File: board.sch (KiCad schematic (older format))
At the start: 1 part

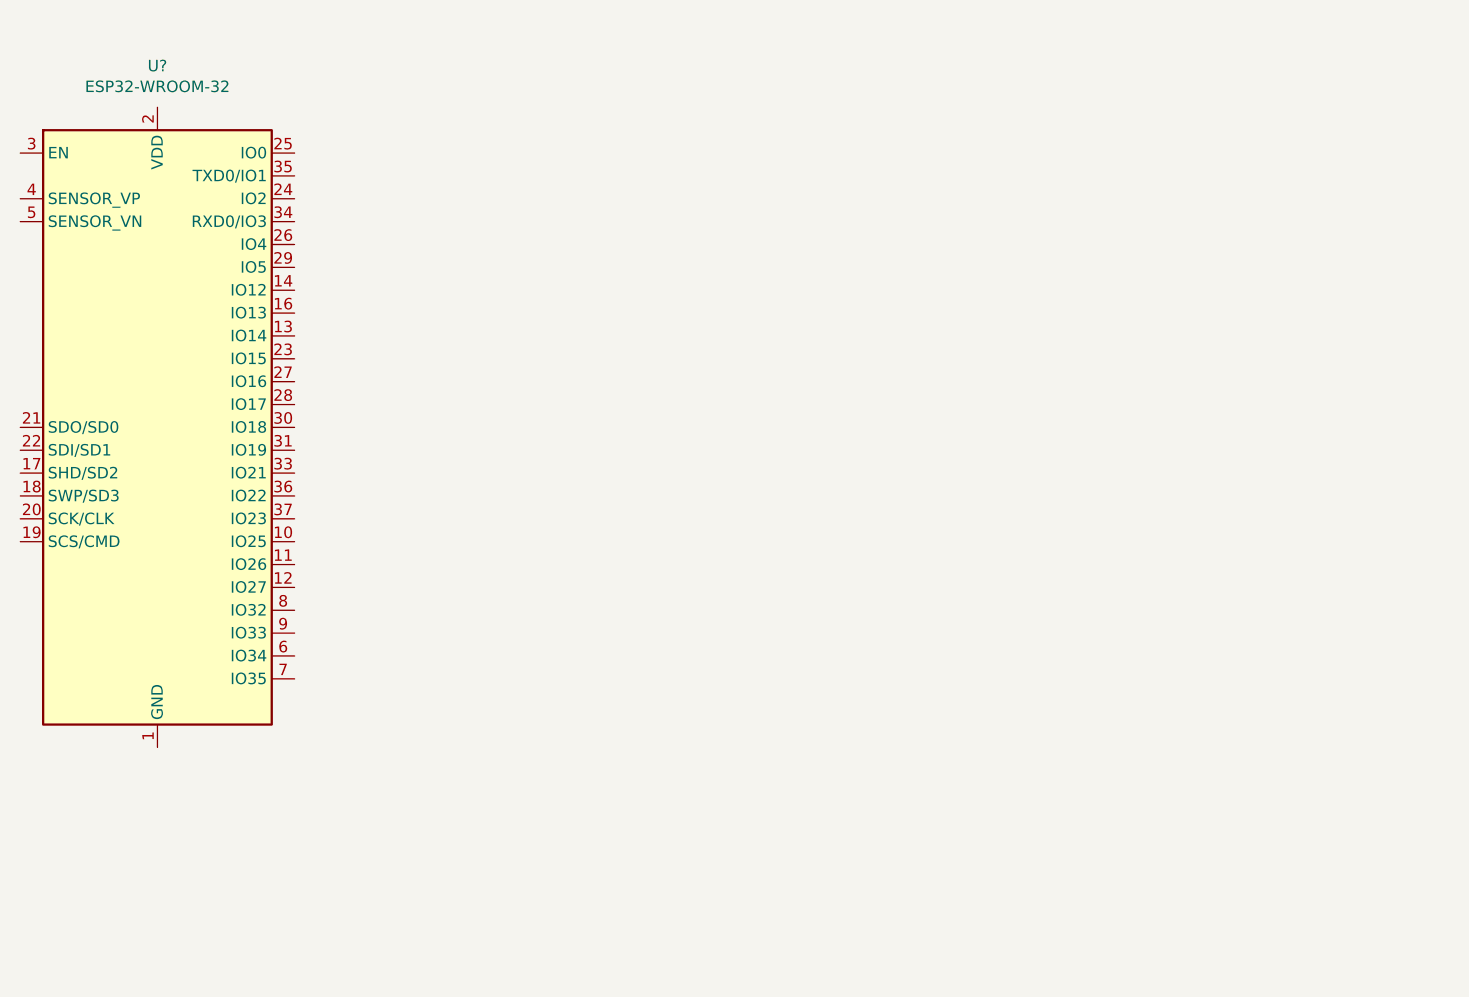
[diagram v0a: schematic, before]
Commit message: added labels
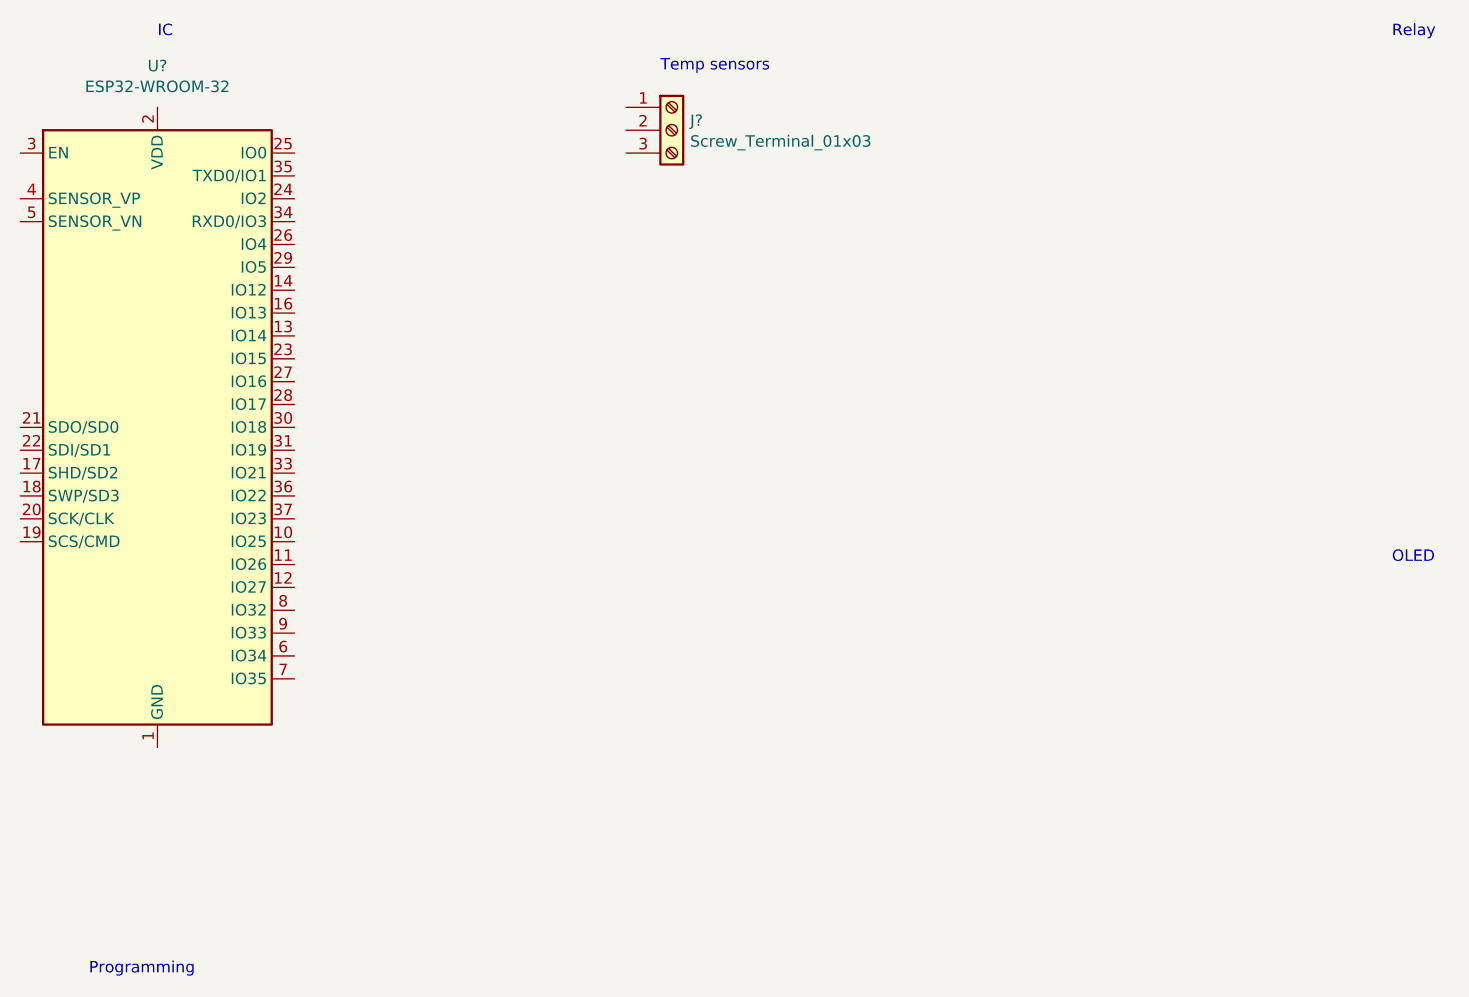
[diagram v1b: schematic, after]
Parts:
- added J?: Screw_Terminal_01x03, symbol Connector:Screw_Terminal_01x03
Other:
- note added: "IC"
- note added: "OLED"
- note added: "Programming"
- note added: "Relay"
- note added: "Temp sensors"
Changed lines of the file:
@@
 	1    0    0    -1
 $EndComp
+$Comp
+L Connector:Screw_Terminal_01x03 J?
+U 1 1 60CDEB35
+P 5950 1750
+F 0 "J?" H 6030 1792 50  0000 L CNN
+F 1 "Screw_Terminal_01x03" H 6030 1701 50  0000 L CNN
+F 2 "" H 5950 1750 50  0001 C CNN
+F 3 "~" H 5950 1750 50  0001 C CNN
+	1    5950 1750
+	1    0    0    -1
+$EndComp
+Text Notes 5900 1500 0    50   ~ 0
+Temp sensors
+Text Notes 3700 1350 0    50   ~ 0
+IC
+Text Notes 9100 1350 0    50   ~ 0
+Relay
+Text Notes 9100 3650 0    50   ~ 0
+OLED
+Text Notes 3400 5450 0    50   ~ 0
+Programming
 $EndSCHEMATC

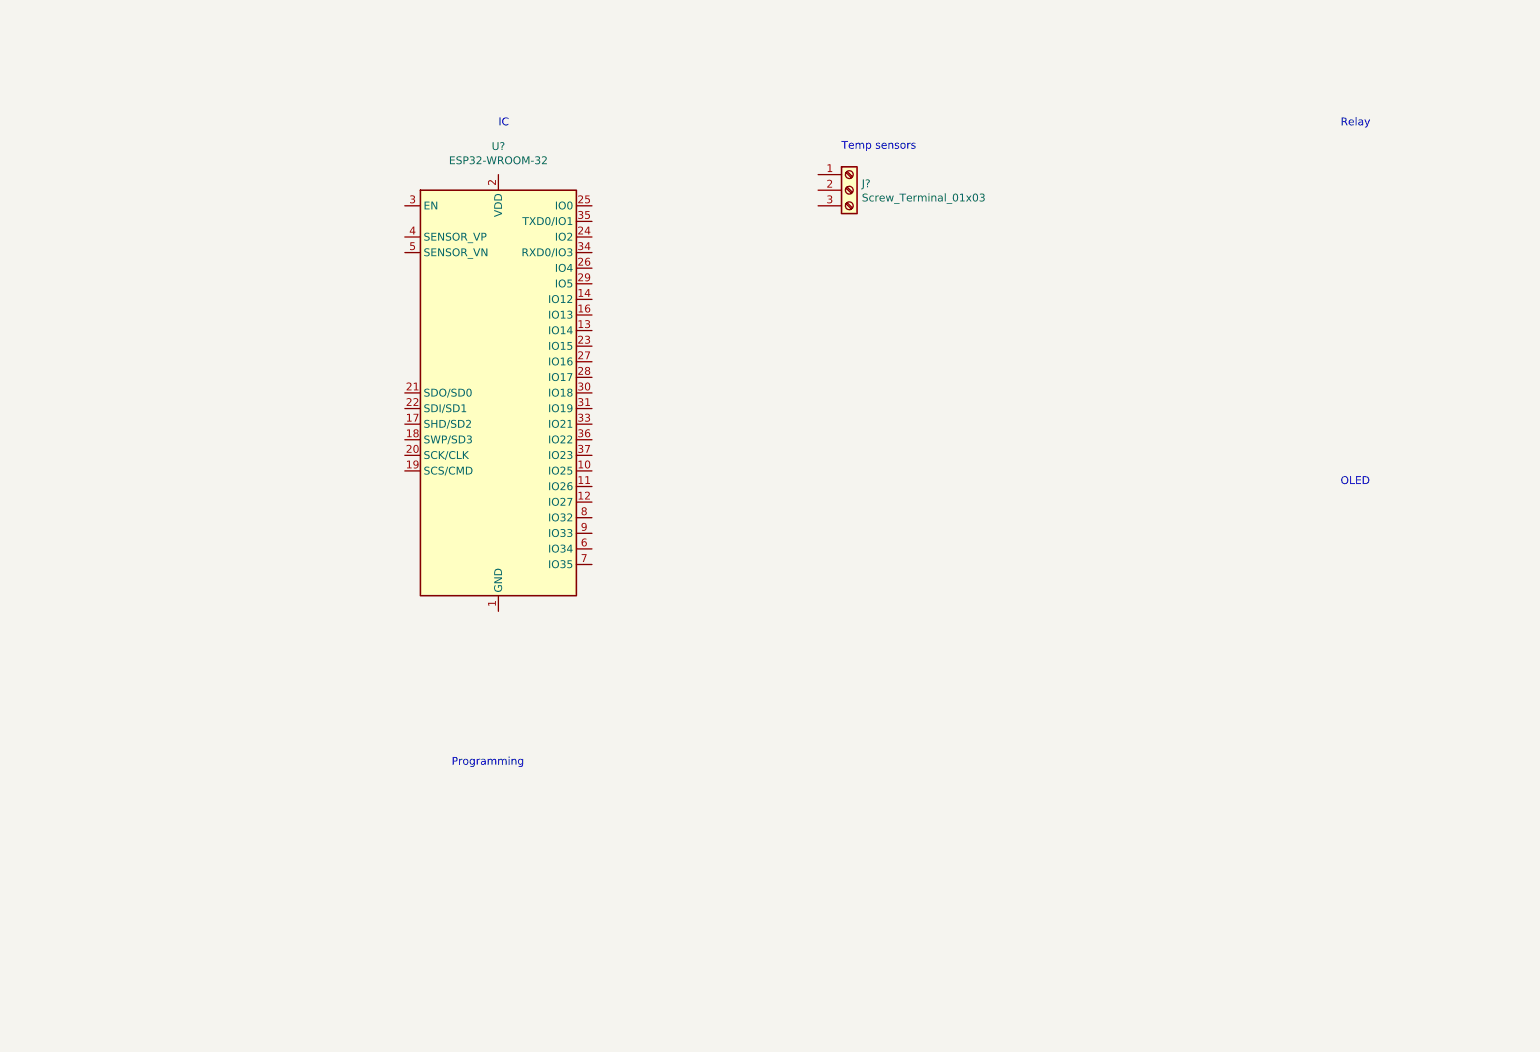
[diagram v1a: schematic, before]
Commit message: initial fiddling with 3d board view
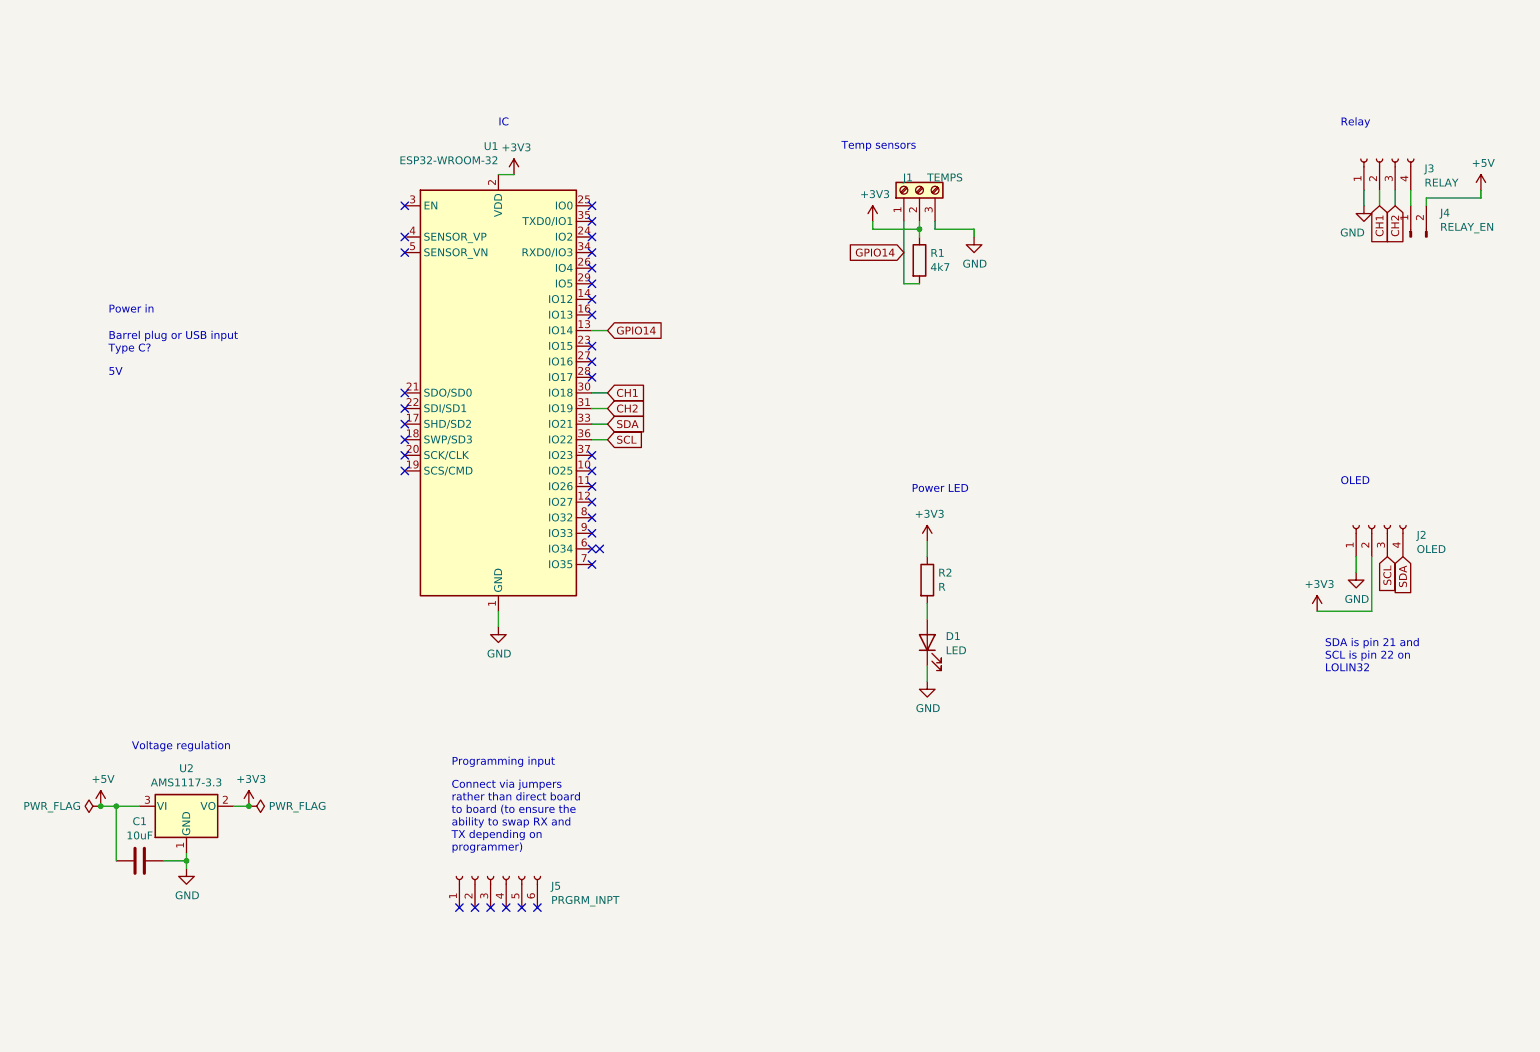
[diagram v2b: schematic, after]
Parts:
- added C1: 10uF, Capacitor_SMD:CP_Elec_3x5.3, symbol Device:C
- added D1: LED, LED_SMD:LED_0201_0603Metric, symbol Device:LED
- added J2: OLED, Connector_JST:JST_EH_B4B-EH-A_1x04_P2.50mm_Vertical, symbol Connector:Conn_01x04_Female
- added J3: RELAY, Connector_JST:JST_EH_B4B-EH-A_1x04_P2.50mm_Vertical, symbol Connector:Conn_01x04_Female
- added J4: RELAY_EN, Connector_PinHeader_2.54mm:PinHeader_1x02_P2.54mm_Vertical, symbol Connector:Conn_01x02_Male
- added J5: PRGRM_INPT, Connector_PinHeader_2.54mm:PinHeader_1x06_P2.54mm_Vertical, symbol Connector:Conn_01x06_Female
- added R1: 4k7, Resistor_SMD:R_0201_0603Metric, symbol Device:R
- added R2: R, Resistor_SMD:R_0201_0603Metric, symbol Device:R
- added U2: AMS1117-3.3, Package_TO_SOT_SMD:SOT-223-3_TabPin2, symbol Regulator_Linear:AMS1117-3.3
- J1: renamed from J?; value Screw_Terminal_01x03 -> TEMPS; footprint (none) -> Connector_JST:JST_EH_S3B-EH_1x03_P2.50mm_Horizontal
- gave numbers to parts that had none: 1
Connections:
- net GND: now reaches U1.1 (GND), U1.15 (GND), U1.38 (GND), U1.39 (GND)
- net GND: now also J1.3 (Pin_3), C1.1, D1.1 (K), J2.1 (Pin_1), J3.1 (Pin_1), U2.1 (GND)
- net GPIO14: now reaches U1.13 (IO14)
- net GPIO14: now also J1.1 (Pin_1), R1.2
- net +3V3: now reaches U1.2 (VDD)
- net +3V3: now also J1.2 (Pin_2), J2.2 (Pin_2), R1.1, R2.1, U2.2 (VO)
- net CH1: now reaches U1.30 (IO18)
- net CH1: now also J3.2 (Pin_2)
- net CH2: now reaches U1.31 (IO19)
- net CH2: now also J3.3 (Pin_3)
- net SDA: now reaches U1.33 (IO21)
- net SDA: now also J2.4 (Pin_4)
- net SCL: now reaches U1.36 (IO22)
- net SCL: now also J2.3 (Pin_3)
- new net: J3.4 (Pin_4), J4.1 (Pin_1)
- new net: D1.2 (A), R2.2
- new net +5V: C1.2, J4.2 (Pin_2), U2.3 (VI)
- no-connect marks 0 -> 35
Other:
- note added: "5V"
- note added: "Barrel plug or USB input\nType C?"
- note added: "Connect via jumpers \nrather than direct board \nto board (to ensure the \nability to swap RX and \nTX depending on \nprogrammer)"
- note added: "Power LED"
- note added: "Power in"
- note added: "Programming input"
- note added: "SDA is pin 21 and \nSCL is pin 22 on \nLOLIN32\n"
- note added: "Voltage regulation"
- note removed: "Programming"
- moved on the sheet: J1

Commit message: added programmer, usb and general design improvements to schematic and did some measuring for final board
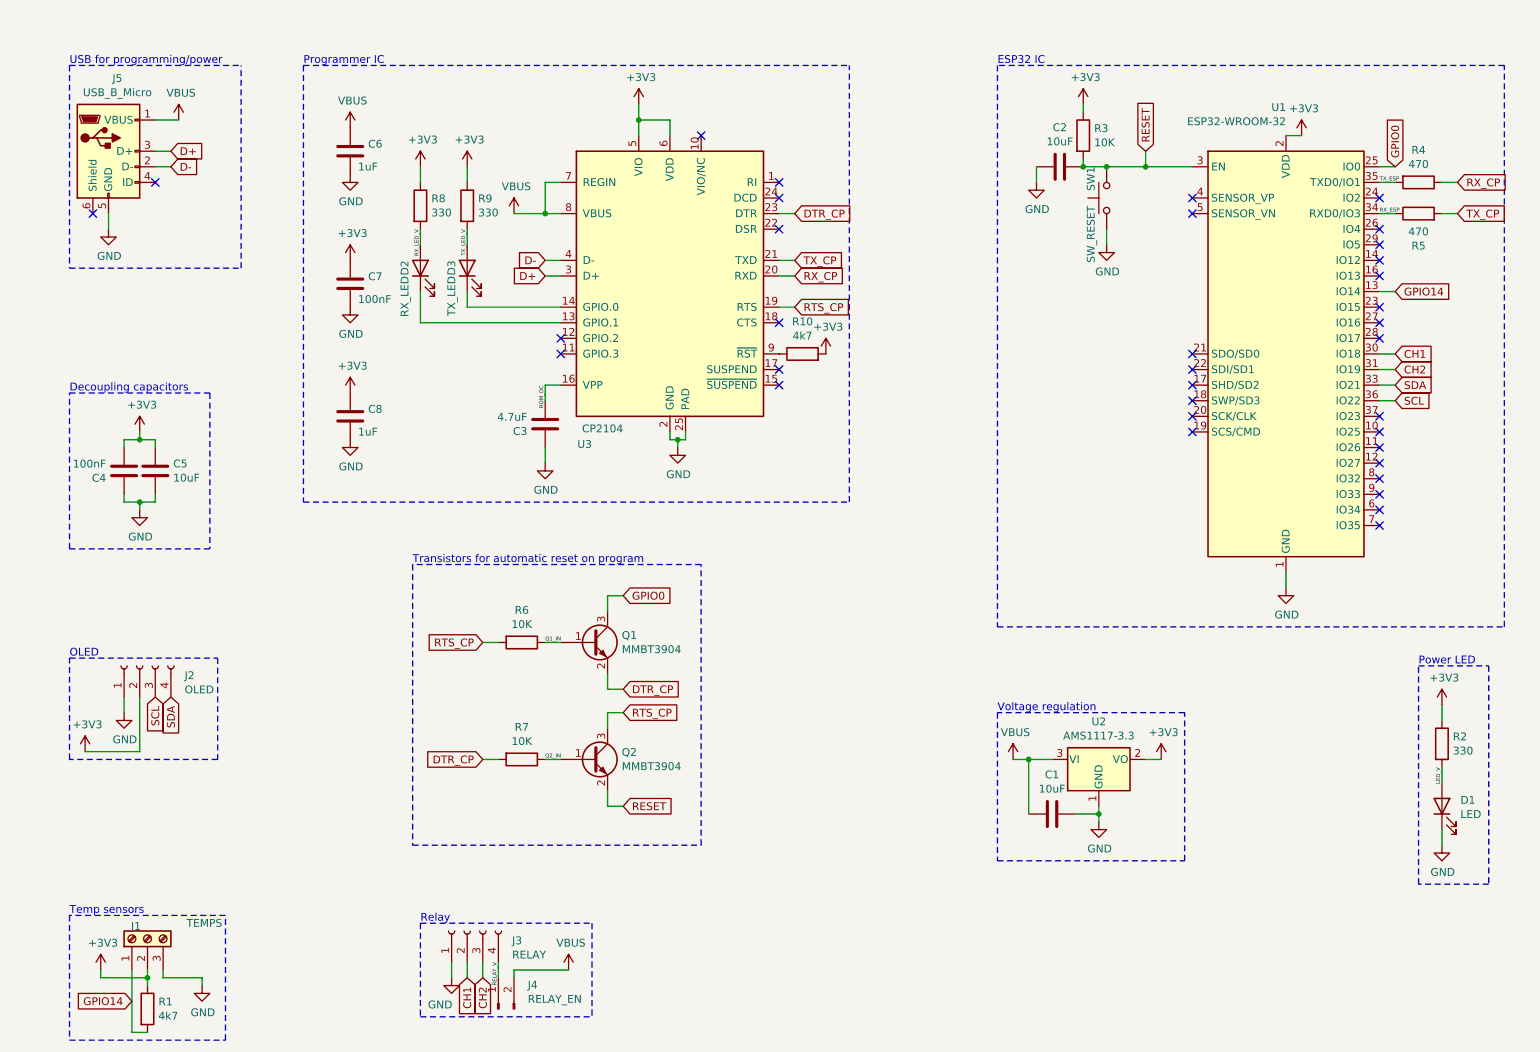
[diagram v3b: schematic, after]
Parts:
- removed J5: PRGRM_INPT, Connector_PinHeader_2.54mm:PinHeader_1x06_P2.54mm_Vertical, symbol Connector:Conn_01x06_Female
- added C2, C5: 10uF, Capacitor_SMD:C_0805_2012Metric, symbol Device:C
- added C3: 4.7uF, Capacitor_SMD:C_0805_2012Metric, symbol Device:C
- added C4, C7: 100nF, Capacitor_SMD:C_0805_2012Metric, symbol Device:C
- added C6, C8: 1uF, Capacitor_SMD:C_0805_2012Metric, symbol Device:C
- added D2: RX_LED, LED_SMD:LED_0805_2012Metric, symbol Device:LED
- added D3: TX_LED, LED_SMD:LED_0805_2012Metric, symbol Device:LED
- added J5: USB_B_Micro, Connector_USB:USB_Micro-B_Molex_47346-0001, symbol Connector:USB_B_Micro
- added Q1, Q2: MMBT3904, Package_TO_SOT_SMD:SOT-23, symbol Transistor_BJT:MMBT3904
- added R10: 4k7, Resistor_SMD:R_0805_2012Metric, symbol Device:R
- added R3, R6, R7: 10K, Resistor_SMD:R_0805_2012Metric, symbol Device:R
- added R4, R5: 470, Resistor_SMD:R_0805_2012Metric, symbol Device:R
- added R8, R9: 330, Resistor_SMD:R_0805_2012Metric, symbol Device:R
- added SW1: SW_RESET, Button_Switch_SMD:SW_SPST_B3U-1000P-B, symbol Switch:SW_Push
- added U3: CP2104, Package_DFN_QFN:QFN-24-1EP_4x4mm_P0.5mm_EP2.6x2.6mm, symbol Interface_USB:CP2104
- C1: footprint Capacitor_SMD:CP_Elec_3x5.3 -> Capacitor_SMD:C_0805_2012Metric
- D1: footprint LED_SMD:LED_0201_0603Metric -> LED_SMD:LED_0805_2012Metric
- J1: footprint Connector_JST:JST_EH_S3B-EH_1x03_P2.50mm_Horizontal -> Connector_JST:JST_XH_B3B-XH-A_1x03_P2.50mm_Vertical
- J2, J3: footprint Connector_JST:JST_EH_B4B-EH-A_1x04_P2.50mm_Vertical -> Connector_JST:JST_XH_B4B-XH-A_1x04_P2.50mm_Vertical
- R1: footprint Resistor_SMD:R_0201_0603Metric -> Resistor_SMD:R_0805_2012Metric
- R2: value R -> 330; footprint Resistor_SMD:R_0201_0603Metric -> Resistor_SMD:R_0805_2012Metric
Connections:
- net +3V3: now also C4.2, C5.1, C7.1, C8.1, R10.2, R3.1, R8.1, R9.1, U3.5 (VIO), U3.6 (VDD)
- net GND: now also C2.1, C3.2, C4.1, C5.2, C6.2, C7.2, C8.2, J5.5 (GND), SW1.1, U3.2 (GND), U3.25 (PAD)
- net GPIO0: now reaches U1.25 (IO0)
- net GPIO0: now also Q1.3 (C)
- net RESET: now reaches U1.3 (EN)
- net RESET: now also C2.2, Q2.2 (E), R3.2, SW1.2
- net RX_ESP: now reaches U1.34 (RXD0/IO3)
- net RX_ESP: now also R5.1
- net TX_ESP: now reaches U1.35 (TXD0/IO1)
- net TX_ESP: now also R4.2
- net RELAY_V: now reaches J3.4 (Pin_4), J4.1 (Pin_1)
- net LED_V: now reaches D1.2 (A), R2.2
- net +5V renamed VBUS
- net VBUS: now also C6.1, J5.1 (VBUS), U3.7 (REGIN), U3.8 (VBUS)
- new net: D2.1 (K), U3.13 (GPIO.1)
- new net: D3.1 (K), U3.14 (GPIO.0)
- new net: R10.1, U3.9 (~RST)
- new net D+: J5.3 (D+), U3.3 (D+)
- new net D-: J5.2 (D-), U3.4 (D-)
- new net DTR_CP: Q1.2 (E), R7.2, U3.23 (DTR)
- new net Q1_IN: Q1.1 (B), R6.1
- new net Q2_IN: Q2.1 (B), R7.1
- new net ROM_DC: C3.1, U3.16 (VPP)
- new net RTS_CP: Q2.3 (C), R6.2, U3.19 (RTS)
- new net RX_CP: R4.1, U3.20 (RXD)
- new net RX_LED_V: D2.2 (A), R8.2
- new net TX_CP: R5.2, U3.21 (TXD)
- new net TX_LED_V: D3.2 (A), R9.2
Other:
- note added: "Decoupling capacitors"
- note added: "ESP32 IC"
- note added: "Programmer IC"
- note added: "Transistors for automatic reset on program"
- note added: "USB for programming/power"
- note removed: "5V"
- note removed: "Barrel plug or USB input\nType C?"
- note removed: "Connect via jumpers \nrather than direct board \nto board (to ensure the \nability to swap RX and \nTX depending on \nprogrammer)"
- note removed: "IC"
- note removed: "Power in"
- note removed: "Programming input"
- note removed: "SDA is pin 21 and \nSCL is pin 22 on \nLOLIN32\n"
- moved on the sheet: C1, D1, J1, J2, J3, J4, R1, R2, U1, U2
